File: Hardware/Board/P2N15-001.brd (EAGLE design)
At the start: 72 x 72 mm, 31 parts, among them IC1 TLC5941NT, IC2 LTC485N, IC3 74LS07N, IC4 LTC485N, X1 HIROSE-DX10LM1-14SE

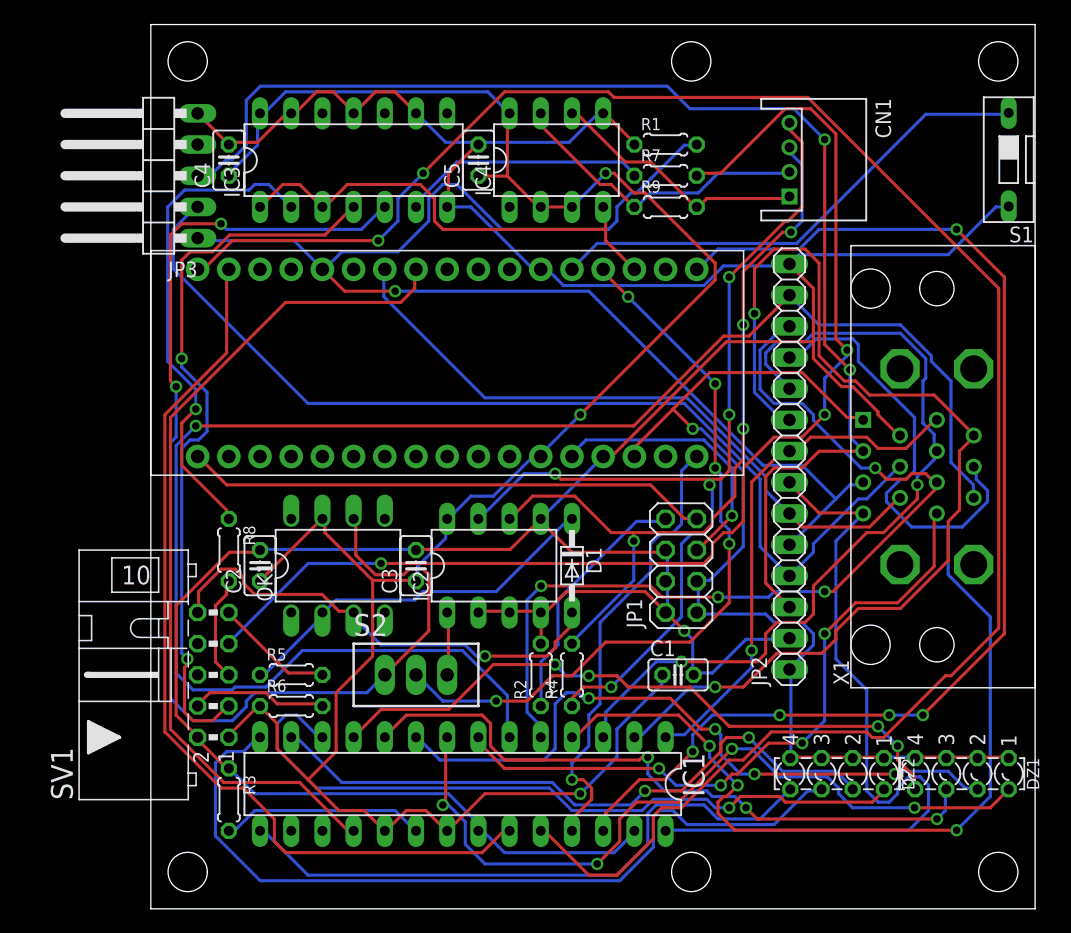
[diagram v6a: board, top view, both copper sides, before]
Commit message: Changed 10p-backport to 14p-backport.
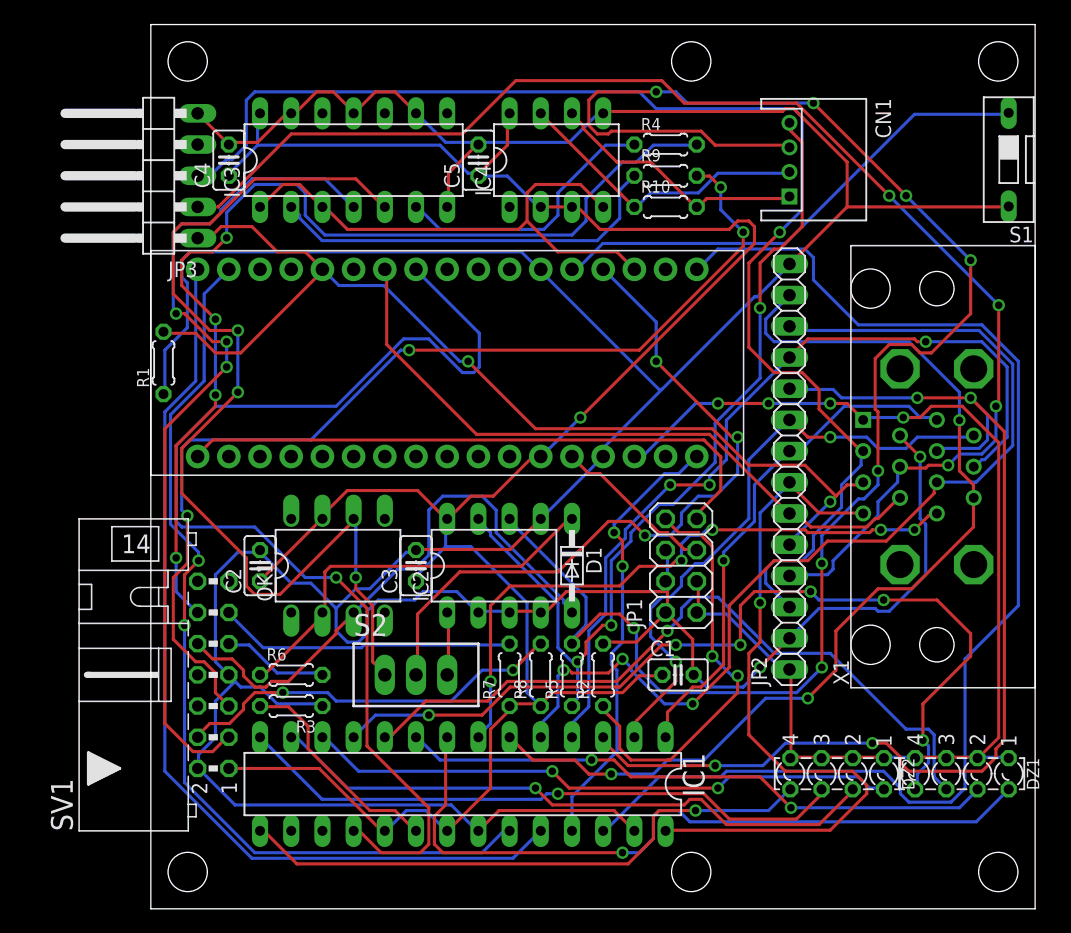
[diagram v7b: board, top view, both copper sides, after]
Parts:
- added R10: 120, resistor:0204/5
- R4, R9: value 120 -> 220
- R5: value 220 -> 120
- SV1: device con-ml:ML10L -> con-ml:ML14L
- moved R1 44.6 mm to (1.03, 44.5), turned to 90 degrees
- moved R4 43.8 mm to (41.9, 62.2), turned to 0 degrees
- moved R7 42.6 mm to (29.2, 19.1), turned to 90 degrees
- moved R8 27.4 mm to (31.8, 19.1), turned to 90 degrees
- moved R5 22.9 mm to (34.3, 19.1), turned to 90 degrees
- moved R3 9.16 mm to (11.4, 16.5), turned to 180 degrees
- moved R2 5.08 mm to (36.8, 19.1)
- moved R6 2.54 mm to (11.4, 19.1)
- moved R9 2.54 mm to (41.9, 59.7)
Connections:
- new net N$10: R4.2, SV1.12
- net GND: now also SV1.7
- net N$15: now also R6.1; no longer R5.1
- net N$2: now also R9.1; no longer R8.1
- net N$6: now also R4.1; no longer R7.1
- net N$7: now also SV1.11; no longer SV1.7
- net RETURN: now also R9.2; no longer R8.2
- net RX+: now also R5.2; no longer R4.2
- net RX-: now also R5.1; no longer R4.1
- net RXA: now also R6.2; no longer R5.2
- net SEND: now also R8.2; no longer R6.2
- net TX+: now also R10.2; no longer R9.2
- net TX-: now also R10.1; no longer R9.1
- net VCC: now also R7.1, R8.1; no longer R6.1
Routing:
- net N$10: track 0.00 -> 84.5 mm, vias 0 -> 4
- net GPIO2: track 155.2 -> 76.4 mm, vias 2 -> 0
- net GND: track 284.3 -> 361.0 mm, vias 1 -> 2
- net RETURN: track 8.54 -> 84.4 mm, vias 0 -> 4
- net N$7: track 97.8 -> 24.2 mm, vias 3 -> 0
- net RX+: track 64.5 -> 137.9 mm, vias 4 -> 8
- net N$29: track 134.0 -> 82.3 mm, vias 1 -> 3
- net ANLG1: track 86.1 -> 50.1 mm
- net ANLG3: track 103.2 -> 68.9 mm
- net USBD-: track 82.7 -> 111.4 mm, vias 0 -> 4
- net GPIO0: track 69.5 -> 92.8 mm, vias 0 -> 1
- net PD: track 108.4 -> 86.3 mm, vias 1 -> 2
- net ANLG2: track 68.0 -> 90.0 mm, vias 2 -> 4
- net SEND: track 11.2 -> 32.0 mm, vias 0 -> 2
- net LED3: track 53.6 -> 73.4 mm, vias 4 -> 6
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
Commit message: Reset of P2N15-001.{brd,sch}.
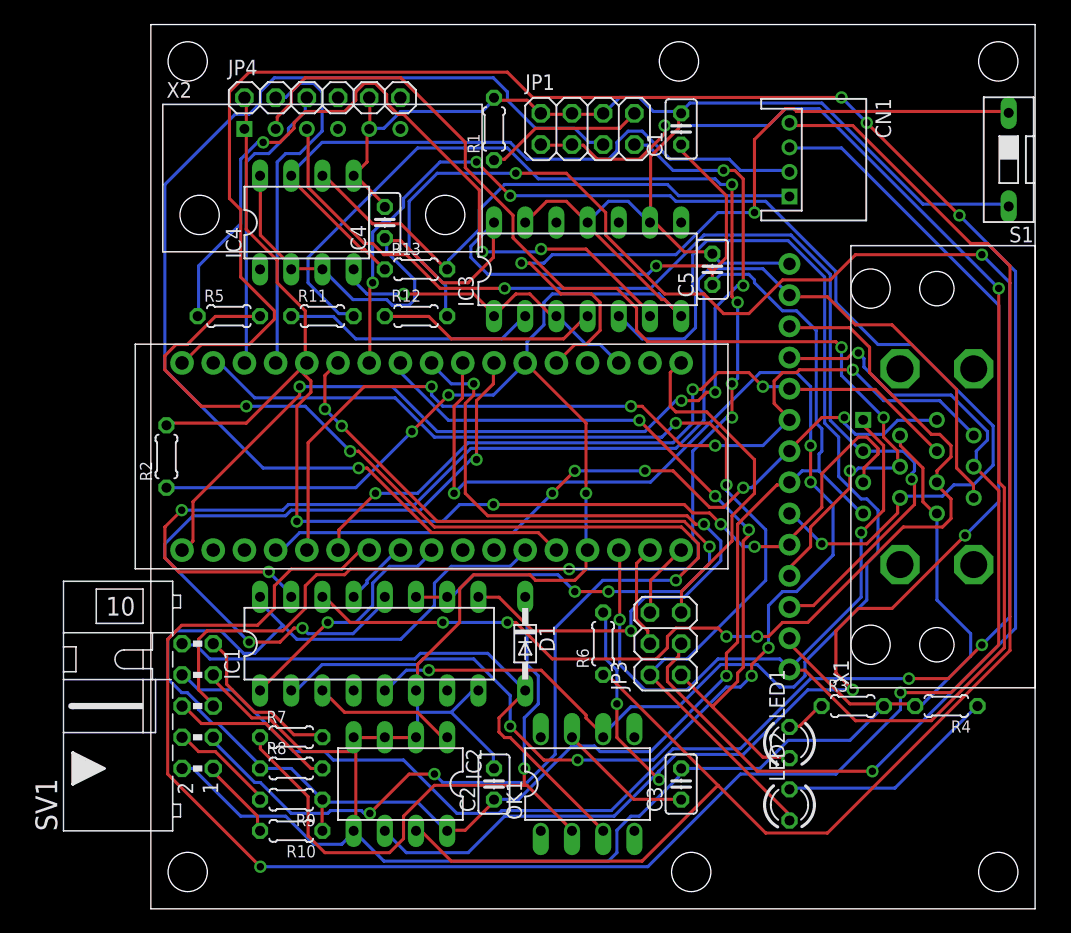
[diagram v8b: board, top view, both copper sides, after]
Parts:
- removed DZ1, DZ2: LZR184, led:LZR184
- removed S2: TL36PO, switch:TL3XPO
- added JP4: (no value), adafruit:1X06
- added LED1, LED2: (no value), led:LED3MM
- added R11, R12: 220, resistor:0204/5
- added R13: 120, resistor:0204/5
- added X2: SUNHAYATO-USB-CK37, con-sunhayato-usb:SUNHAYATO-USB-CK37
- IC1: value TLC5941NT -> 4053N; device adafruit:DIL28-3 -> 40xx:DIL16
- JP2: device pinhead:1X14 -> adafruit:1X14-CB
- JP3: device pinhead:1X05/90 -> pinhead:2X03
- R1: value 10k -> 150
- R10, R5: value 120 -> 220
- R2: value 150 -> 10k
- R3: value 4.7k -> 330
- R4: value 220 -> 330
- R6: value 220 -> 120
- SV1: device con-ml:ML14L -> con-ml:ML10L
- moved R10 59.2 mm to (11.4, 6.35), turned to 180 degrees
- moved R9 59.2 mm to (11.4, 8.89), turned to 180 degrees
- moved JP3 56.6 mm to (41.9, 21.6)
- moved R4 51.1 mm to (64.8, 16.5), turned to 180 degrees
- moved R3 45.7 mm to (57.1, 16.5), turned to 0 degrees
- moved C1 44.5 mm to (43.2, 63.5), turned to 90 degrees
- moved R5 40.4 mm to (6.35, 48.3), turned to 0 degrees
- moved R2 39.8 mm to (1.27, 36.8)
- moved JP1 36.4 mm to (35.6, 63.5), turned to 0 degrees
- moved R1 33.0 mm to (27.9, 63.5)
- moved C3 28.0 mm to (43.2, 10.2)
- moved OK1 27.0 mm to (35.6, 10.2)
- moved C2 26.1 mm to (27.9, 10.2)
- moved R6 25.5 mm to (36.8, 21.6), turned to 90 degrees
- moved R8 21.7 mm to (11.4, 11.4), turned to 0 degrees
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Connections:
- removed net LED0: DZ1.K1, IC1.8
- removed net LED1: DZ1.K2, IC1.9
- removed net LED2: DZ1.K3, IC1.10
- removed net LED3: DZ1.K4, IC1.11
- removed net LED4: DZ2.K1, IC1.12
- removed net LED5: DZ2.K2, IC1.13
- removed net LED6: DZ2.K3, IC1.14
- removed net LED7: DZ2.K4, IC1.15
- removed net N$1 (its old number): IC1.28, JP2.7, X1.P$7
- removed net N$10: R4.2, SV1.12
- removed net N$7: R7.2, SV1.11
- removed net RAWTX: IC3.4, SV1.3
- removed net RETURN: R9.2, SV1.5
- removed net SEND: R8.2, SV1.4
- new net ANLG4: IC1.13, MC1.P$27
- new net ANLG5: IC1.1, MC1.P$26
- new net MISO: JP3.4, MC1.P$19
- new net N$17: LED1.K, R3.1
- new net N$18: LED2.K, R4.1
- new net N$5: JP4.2, MC1.P$4
- new net RXRETURN: R5.2, SV1.3
- new net RXSEND: R10.2, SV1.1
- new net SCL: IC1.2, MC1.P$10
- new net SDA: IC1.12, MC1.P$11
- new net SEL: IC1.10, IC1.11, MC1.P$6
- new net TX2RETURN: R11.2, SV1.5
- new net TX2SEND: R9.2, SV1.4
- new net TXRETURN: R12.2, SV1.8
- new net TXSEND: R8.2, SV1.6
- new net VEE: IC1.7
- net ANLG0: now also MC1.P$31; no longer IC1.1
- net ANLG1: now also MC1.P$30; no longer IC1.2
- net ANLG2: now also MC1.P$29; no longer IC1.3
- net ANLG3: now also MC1.P$28; no longer IC1.4
- net GND: now also IC1.6, IC1.8, JP4.5, R1.2, R2.1, R3.2, R4.2, X1.P$14, X2.P$5; no longer IC1.22, IC1.27, JP3.5, R1.1, R2.2, R3.1
- net GPIO0: now also JP3.1, LED1.A; no longer IC1.18
- net GPIO1: now also JP3.2, LED2.A; no longer IC1.23
- net GPIO2: now also JP3.3; no longer IC1.24
- net MIDIRX: now also IC1.5; no longer S2.1
- net MOSI: now also JP3.5; no longer IC1.26
- net N$15: now also R7.1; no longer R6.1
- net N$2: now also R11.1; no longer R9.1
- net N$28: now also IC1.14; no longer IC1.5
- net N$29: now also IC1.15; no longer IC1.6
- net N$3: now also IC3.6, R5.1; no longer MC1.P$4
- net N$32: now also R1.1; no longer R2.1
- net N$4: now also IC3.4, R12.1; no longer IC1.20, R3.2
- net N$6: now also JP4.3, MC1.P$3; no longer IC3.6, R4.1
- net N$8: now also IC1.9, MC1.P$9; no longer IC1.7, X1.P$14
- net PD: now also JP4.1, R2.2, X2.P$1; no longer JP3.1, R1.2
- net RX: no longer S2.2
- net RX+: now also R6.2; no longer R5.2
- net RX-: now also R6.1; no longer R5.1
- net RXA: now also R7.2; no longer R6.2
- net SCLK: now also JP3.6; no longer IC1.25
- net TX+: now also R13.2; no longer R10.2
- net TX-: now also R13.1; no longer R10.1
- net USBD+: now also X2.P$3; no longer JP3.3
- net USBD-: now also X2.P$2; no longer JP3.2
- net VCC: now also IC1.16, JP2.7, R10.1, R9.1, X1.P$7; no longer IC1.19, IC1.21, R7.1, SV1.1
- net VDD: no longer DZ1.A1, DZ1.A2, DZ1.A3, DZ1.A4, DZ2.A1, DZ2.A2, DZ2.A3, DZ2.A4
- net XMIDIRX: now also IC1.3; no longer S2.3
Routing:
- net TXRETURN: track 0.00 -> 175.1 mm, vias 0 -> 4
- net TX2RETURN: track 0.00 -> 129.4 mm, vias 0 -> 5
- net SCL: track 0.00 -> 118.5 mm, vias 0 -> 7
- net RXRETURN: track 0.00 -> 118.4 mm, vias 0 -> 5
- net GPIO2: track 76.4 -> 169.2 mm, vias 0 -> 4
- net N$10: track 84.5 -> 0.00 mm, vias 4 -> 0
- net RETURN: track 84.4 -> 0.00 mm, vias 4 -> 0
- net RST: track 13.3 -> 95.6 mm, vias 0 -> 1
- net ANLG3: track 68.9 -> 148.7 mm
- net MOSI: track 101.5 -> 27.5 mm
- net LED3: track 73.4 -> 0.00 mm, vias 6 -> 0
- net RAWTX: track 69.1 -> 0.00 mm, vias 3 -> 0
- net SEL: track 0.00 -> 67.8 mm, vias 0 -> 5
- net N$3: track 0.00 -> 62.2 mm, vias 0 -> 3
- net SDA: track 0.00 -> 60.7 mm, vias 0 -> 3
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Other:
- board text added: "PINEAPPLE II NITROGEN 14 REVISION 1.0.0 (2015)"
- board text removed: "PINEAPPLE II NITROGEN 15 REVISION 1.0.0 (2015)"
